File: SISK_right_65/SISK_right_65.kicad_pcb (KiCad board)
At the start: 2 copper layers, 194.5 x 121.8 mm, 93 parts, among them J1 OLED_128x32, J2 Battery Conn, J3 alternative on/off SW (wired), SW1 "6", SW10 "Z", SW11 "U", SW12 "I", SW13 "O", SW14 "P", SW15 "Ü", SW16 "*", SW17 "Enter", SW18 "Del", SW19 "H", SW2 "7", SW20 "J", SW21 "K", SW22 "L", SW23 "Ö", SW24 "Ä", SW25 "'", SW26 "PGUP", SW27 "N", SW28 "M", SW29 ";", SW3 "8", SW30 ":", SW31 "-", SW32 "shift_R", SW33 "UP", SW34 "PGDOWN", SW35 "SPACE_R", SW36 "Alt", SW37 FN, SW38 "Ctrl", SW39 "Left", SW4 "9", SW40 "Down", SW41 "Right", SW5 "0", SW6 "ß", SW7 "`", SW8 "Backspace", SW9 "^", U1 Nice_Nano_V2

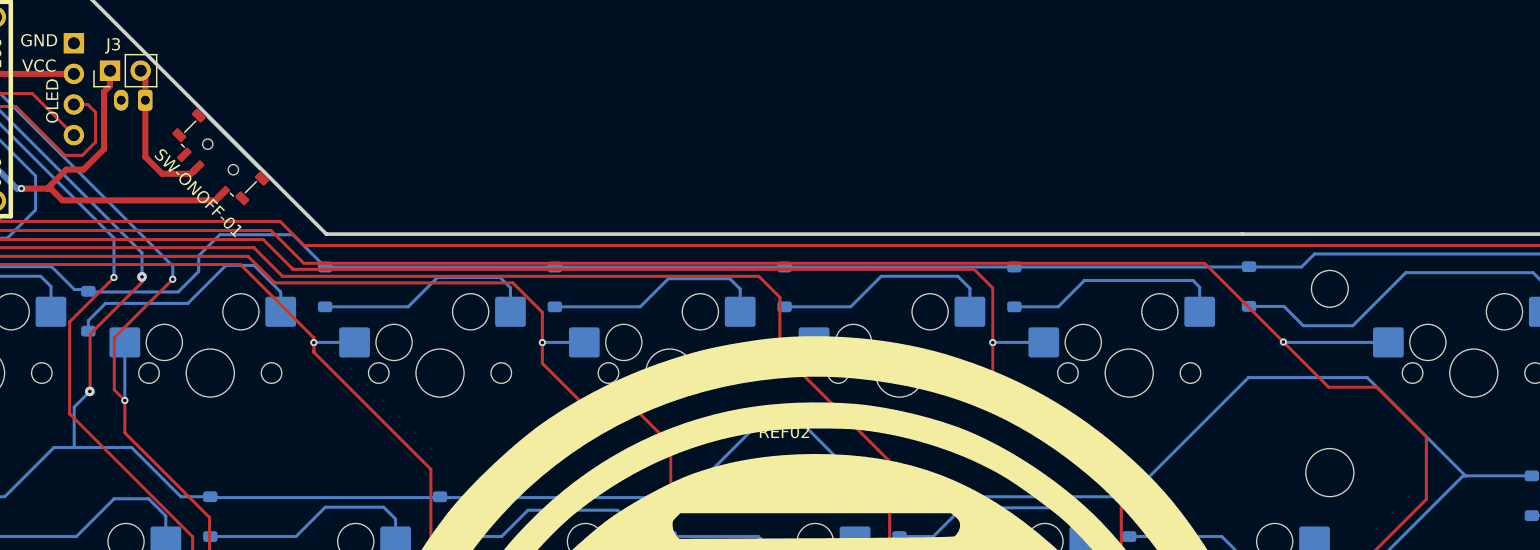
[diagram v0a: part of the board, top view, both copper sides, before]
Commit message: fixed schematics, added optional pullup resistors
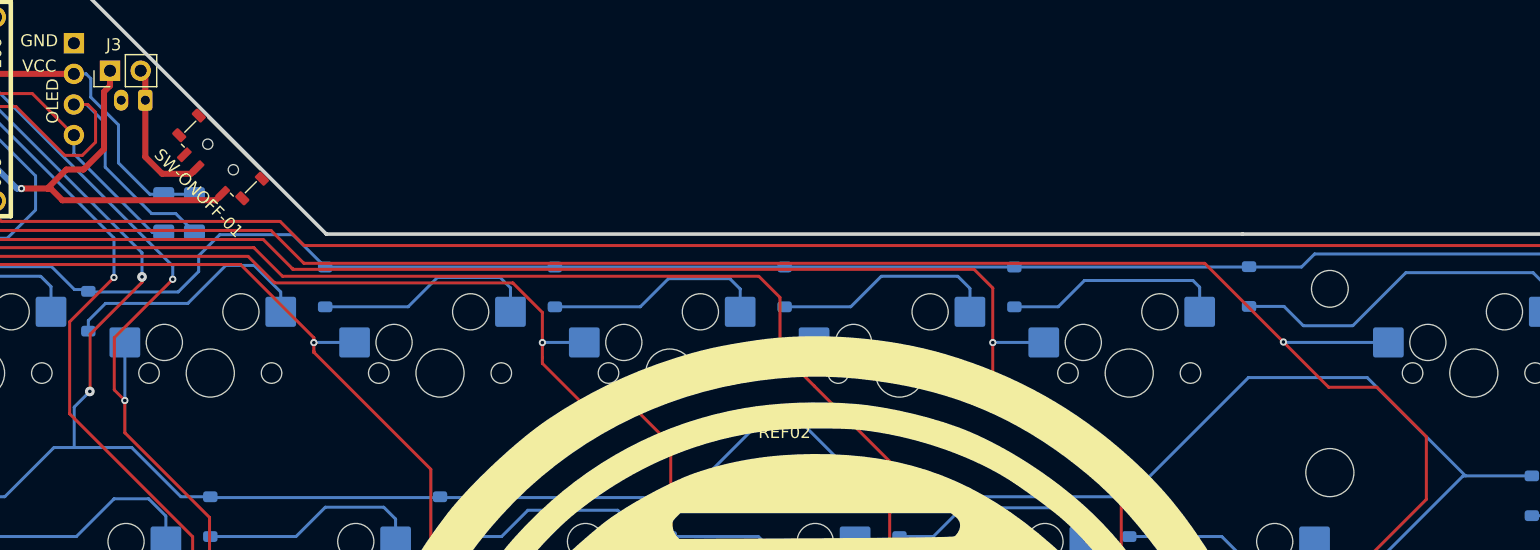
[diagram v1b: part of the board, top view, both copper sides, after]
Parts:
- added R1: 5K, Resistor_SMD:R_1206_3216Metric_Pad1.30x1.75mm_HandSolder, B.Cu at (86.7, 51.8)
- added R2: 5K, Resistor_SMD:R_1206_3216Metric_Pad1.30x1.75mm_HandSolder, B.Cu at (89.2, 51.8)
- J2: value Battery Conn -> Conn
- J3: value alternative on/off SW (wired) -> SWITCH
- SW-ONOFF-01: value onboard ON/OFF SW -> ~
- SW1: value "6" -> SW_push
- SW10: value "Z" -> SW_push
- SW11: value "U" -> SW_push
- SW12: value "I" -> SW_push
- SW13: value "O" -> SW_push
- SW14: value "P" -> SW_push
- SW15: value "Ü" -> SW_push
- SW16: value "*" -> SW_push
- SW17: value "Enter" -> SW_push
- SW18: value "Del" -> SW_push
- SW19: value "H" -> SW_push
- SW2: value "7" -> SW_push
- SW20: value "J" -> SW_push
- SW21: value "K" -> SW_push
- SW22: value "L" -> SW_push
- SW23: value "Ö" -> SW_push
- SW24: value "Ä" -> SW_push
- SW25: value "'" -> SW_push
- SW26: value "PGUP" -> SW_push
- SW27: value "N" -> SW_push
- SW28: value "M" -> SW_push
- SW29: value ";" -> SW_push
- SW3: value "8" -> SW_push
- SW30: value ":" -> SW_push
- SW31: value "-" -> SW_push
- SW32: value "shift_R" -> SW_push
- SW33: value "UP" -> SW_push
- SW34: value "PGDOWN" -> SW_push
- SW35: value "SPACE_R" -> SW_push
- SW36: value "Alt" -> SW_push
- SW37: value FN -> SW_push
- SW38: value "Ctrl" -> SW_push
- SW39: value "Left" -> SW_push
- SW4: value "9" -> SW_push
- SW40: value "Down" -> SW_push
- SW41: value "Right" -> SW_push
- SW5: value "0" -> SW_push
- SW6: value "ß" -> SW_push
- SW7: value "`" -> SW_push
- SW8: value "Backspace" -> SW_push
- SW9: value "^" -> SW_push
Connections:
- net Net-(J1-SCL) renamed /SCL
- net Net-(J1-SDA) renamed /SDA
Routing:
- net VCC: track 30.1 -> 47.2 mm
- net /SCL: track 34.4 -> 50.9 mm
- net /SDA: track 30.8 -> 42.5 mm

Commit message: fixed some issues
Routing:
- net /COL2: track 158.2 -> 157.3 mm
- net GND: vias 0 -> 24

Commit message: fixed most of issues, updated 60% version
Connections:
- net +3.3V renamed +BATT
- net Net-(J3-Pin_1) renamed +VDC
- net VCC renamed +3,3V

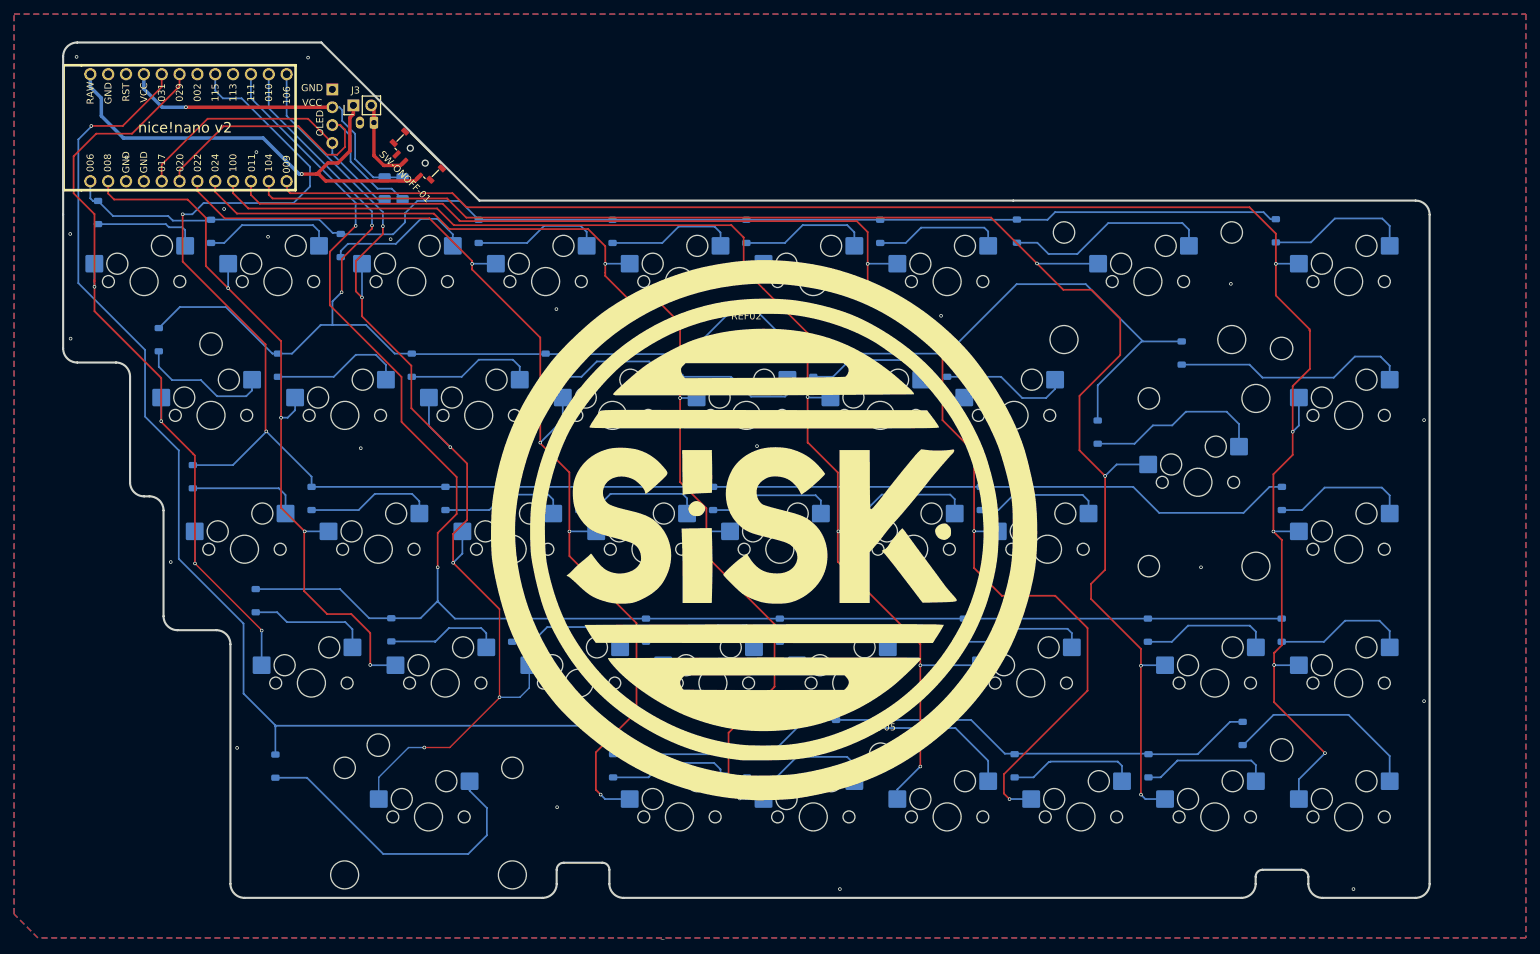
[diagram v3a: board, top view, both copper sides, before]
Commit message: improved the whole mounting hole situation
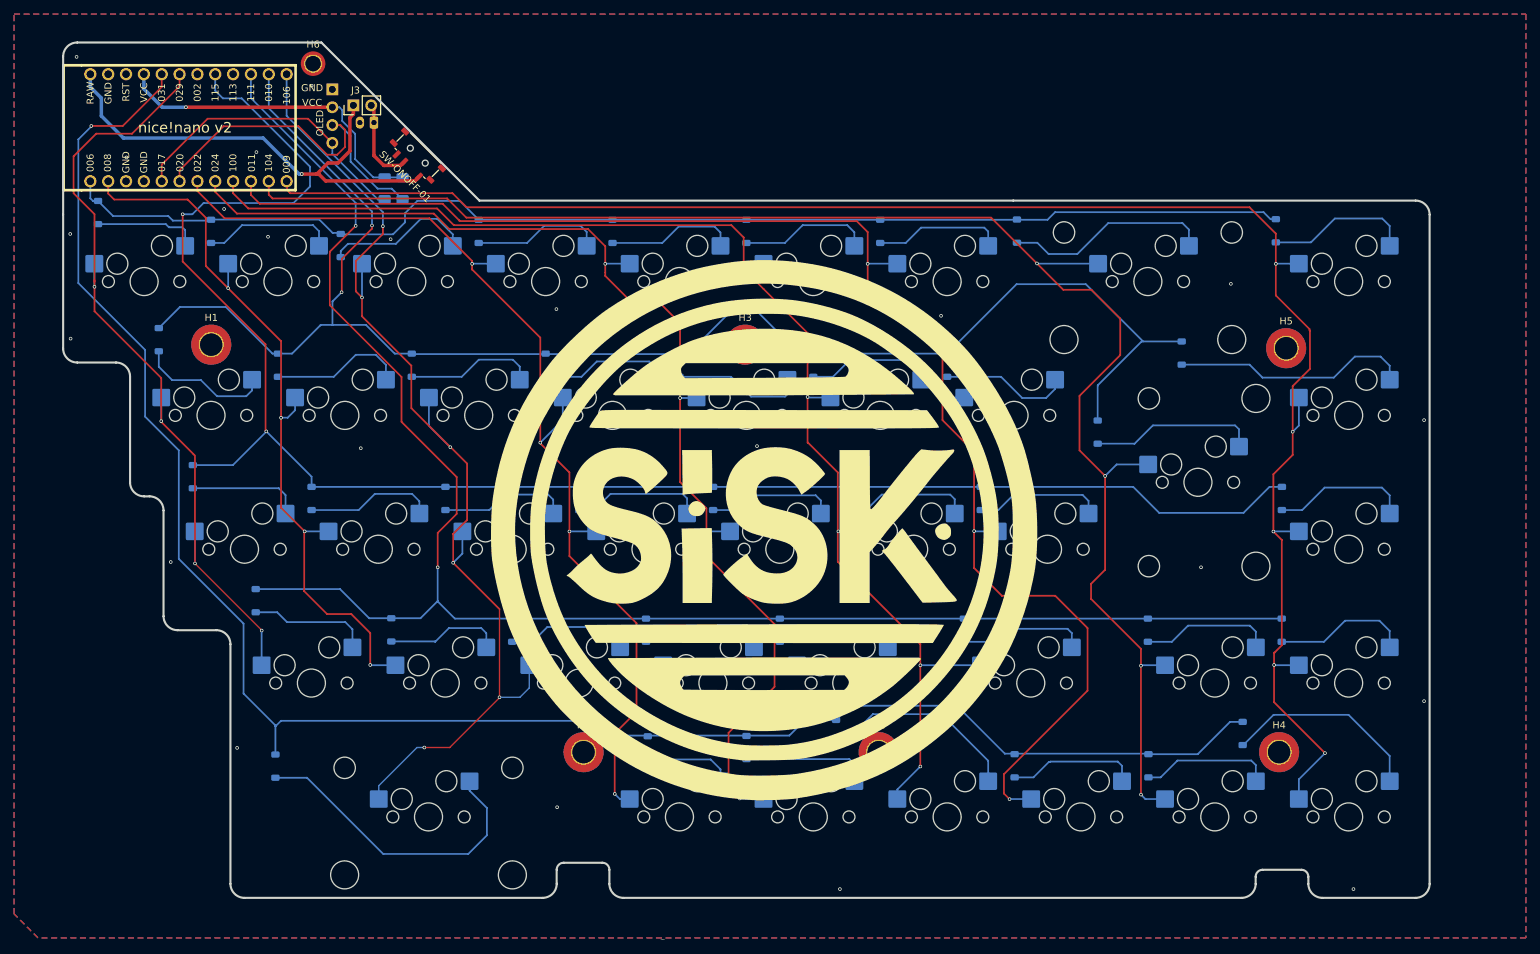
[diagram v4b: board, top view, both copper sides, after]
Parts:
- removed REF01, REF02, REF03, REF04, REF05, REF06: MountingHole_3.2mm_M3_ISO7380, MountingHole:MountingHole_3.2mm_M3_ISO7380
- added H1: M3, MountingHole:MountingHole_3.2mm_M3_ISO7380_Pad_TopBottom, F.Cu at (62.0, 74.0)
- added H2: M3, MountingHole:MountingHole_3.2mm_M3_ISO7380_Pad_TopBottom, F.Cu at (157.0, 132.0)
- added H3: M3, MountingHole:MountingHole_3.2mm_M3_ISO7380_Pad_TopBottom, F.Cu at (138.0, 74.0)
- added H4: M3, MountingHole:MountingHole_3.2mm_M3_ISO7380_Pad_TopBottom, F.Cu at (214.0, 132.0)
- added H5: M3, MountingHole:MountingHole_3.2mm_M3_ISO7380_Pad_TopBottom, F.Cu at (215.0, 74.5)
- added H6: M2, MountingHole:MountingHole_2.2mm_M2_ISO7380_Pad_TopOnly, F.Cu at (76.5, 34.0)
- added H7: M3, MountingHole:MountingHole_3.2mm_M3_ISO7380_Pad_TopBottom, F.Cu at (115.0, 132.0)
- moved D35 5.55 mm to (124.1, 131.4)
- moved D30 2.60 mm to (138.2, 131.3)
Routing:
- net Net-(D35-A): track 18.2 -> 12.6 mm
- net /COL3: track 156.2 -> 152.8 mm
- net Net-(D7-A): track 25.9 -> 23.9 mm
- net Net-(D25-A): track 27.4 -> 29.0 mm
- net Net-(D30-A): track 19.4 -> 18.1 mm
- net /ROW4: track 262.4 -> 261.4 mm
- net /COL2: track 157.3 -> 156.6 mm

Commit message: last changes on silkscreen before manufaturing
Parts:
- J2: value Conn -> Batt
- moved H6 0.50 mm to (77.0, 34.0)
- moved J3 0.10 mm to (82.2, 39.8)
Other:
- outline, holes or cut-outs redrawn
